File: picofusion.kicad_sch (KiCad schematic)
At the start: 35 parts, among them J1 EAST, J2 WEST, J3 SOUTH, J4 NORTH, U1 W25Q16, U2 RP2040, U3 TLV71333PDQNT, Y1 12MHz

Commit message: schematic: add one more decoupling cap for rp2040
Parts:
- added C?: 1uF, Capacitor_SMD:C_0402_1005Metric, symbol Device:C
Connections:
- net +3V3: now also C?.1
- net GND: now also C?.2
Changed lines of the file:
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@@
   (junction (at 204.47 85.09) (diameter 0) (color 0 0 0 0)
   )
+  (junction (at 137.16 24.13) (diameter 0) (color 0 0 0 0)
+  )
   (junction (at 66.04 24.13) (diameter 0.9144) (color 0 0 0 0)
   )
@@
   (junction (at 179.07 85.09) (diameter 0) (color 0 0 0 0)
   )
+  (junction (at 137.16 36.83) (diameter 0) (color 0 0 0 0)
+  )
   (junction (at 71.12 24.13) (diameter 0.9144) (color 0 0 0 0)
   )
+  (junction (at 60.96 24.13) (diameter 0.9144) (color 0 0 0 0)
+  )
+  (junction (at 106.68 24.13) (diameter 0.9144) (color 0 0 0 0)
+  )
+  (junction (at 91.44 170.18) (diameter 0.9144) (color 0 0 0 0)
+  )
+  (junction (at 19.05 36.83) (diameter 0) (color 0 0 0 0)
+  )
+  (junction (at 106.68 36.83) (diameter 0.9144) (color 0 0 0 0)
+  )
+  (junction (at 199.39 85.09) (diameter 0) (color 0 0 0 0)
+  )
+  (junction (at 41.91 162.56) (diameter 0.9144) (color 0 0 0 0)
+  )
+  (junction (at 114.3 24.13) (diameter 0) (color 0 0 0 0)
+  )
+  (junction (at 19.05 24.13) (diameter 0) (color 0 0 0 0)
+  )
+  (junction (at 78.74 170.18) (diameter 0.9144) (color 0 0 0 0)
+  )
+  (junction (at 81.28 24.13) (diameter 0.9144) (color 0 0 0 0)
+  )
+  (junction (at 129.54 36.83) (diameter 0) (color 0 0 0 0)
+  )
+  (junction (at 18.415 177.8) (diameter 0) (color 0 0 0 0)
+  )
+  (junction (at 46.99 24.13) (diameter 0.9144) (color 0 0 0 0)
+  )
+  (junction (at 44.45 24.13) (diameter 0.9144) (color 0 0 0 0)
+  )
+  (junction (at 121.92 24.13) (diameter 0) (color 0 0 0 0)
+  )
+  (junction (at 83.82 24.13) (diameter 0.9144) (color 0 0 0 0)
+  )
+  (junction (at 179.07 87.63) (diameter 0) (color 0 0 0 0)
+  )
+  (junction (at 68.58 24.13) (diameter 0.9144) (color 0 0 0 0)
+  )
   (junction (at 129.54 24.13) (diameter 0) (color 0 0 0 0)
-  )
-  (junction (at 60.96 24.13) (diameter 0.9144) (color 0 0 0 0)
-  )
-  (junction (at 106.68 24.13) (diameter 0.9144) (color 0 0 0 0)
-  )
-  (junction (at 91.44 170.18) (diameter 0.9144) (color 0 0 0 0)
-  )
-  (junction (at 19.05 36.83) (diameter 0) (color 0 0 0 0)
-  )
-  (junction (at 106.68 36.83) (diameter 0.9144) (color 0 0 0 0)
-  )
-  (junction (at 199.39 85.09) (diameter 0) (color 0 0 0 0)
-  )
-  (junction (at 41.91 162.56) (diameter 0.9144) (color 0 0 0 0)
-  )
-  (junction (at 114.3 24.13) (diameter 0) (color 0 0 0 0)
-  )
-  (junction (at 19.05 24.13) (diameter 0) (color 0 0 0 0)
-  )
-  (junction (at 129.54 36.83) (diameter 0) (color 0 0 0 0)
-  )
-  (junction (at 78.74 170.18) (diameter 0.9144) (color 0 0 0 0)
-  )
-  (junction (at 81.28 24.13) (diameter 0.9144) (color 0 0 0 0)
-  )
-  (junction (at 18.415 177.8) (diameter 0) (color 0 0 0 0)
-  )
-  (junction (at 46.99 24.13) (diameter 0.9144) (color 0 0 0 0)
-  )
-  (junction (at 44.45 24.13) (diameter 0.9144) (color 0 0 0 0)
-  )
-  (junction (at 121.92 24.13) (diameter 0) (color 0 0 0 0)
-  )
-  (junction (at 83.82 24.13) (diameter 0.9144) (color 0 0 0 0)
-  )
-  (junction (at 179.07 87.63) (diameter 0) (color 0 0 0 0)
-  )
-  (junction (at 68.58 24.13) (diameter 0.9144) (color 0 0 0 0)
   )
   (junction (at 114.3 36.83) (diameter 0) (color 0 0 0 0)
@@
     (stroke (width 0) (type solid) (color 0 0 0 0))
   )
+  (wire (pts (xy 137.16 36.83) (xy 129.54 36.83))
+    (stroke (width 0) (type default) (color 0 0 0 0))
+  )
   (wire (pts (xy 19.05 36.83) (xy 25.4 36.83))
     (stroke (width 0) (type solid) (color 0 0 0 0))
@@
     (stroke (width 0) (type default) (color 0 0 0 0))
   )
-  (wire (pts (xy 132.08 21.59) (xy 132.08 24.13))
+  (wire (pts (xy 139.7 21.59) (xy 139.7 24.13))
     (stroke (width 0) (type solid) (color 0 0 0 0))
   )
@@
     (stroke (width 0) (type default) (color 0 0 0 0))
   )
-  (wire (pts (xy 132.08 36.83) (xy 132.08 39.37))
+  (wire (pts (xy 139.7 36.83) (xy 139.7 39.37))
     (stroke (width 0) (type default) (color 0 0 0 0))
   )
@@
     (stroke (width 0) (type solid) (color 0 0 0 0))
   )
+  (wire (pts (xy 129.54 24.13) (xy 137.16 24.13))
+    (stroke (width 0) (type default) (color 0 0 0 0))
+  )
   (wire (pts (xy 25.4 36.83) (xy 31.75 36.83))
     (stroke (width 0) (type solid) (color 0 0 0 0))
@@
     (stroke (width 0) (type default) (color 0 0 0 0))
   )
+  (wire (pts (xy 137.16 24.13) (xy 137.16 26.67))
+    (stroke (width 0) (type default) (color 0 0 0 0))
+  )
   (wire (pts (xy 66.04 24.13) (xy 63.5 24.13))
     (stroke (width 0) (type solid) (color 0 0 0 0))
@@
     (stroke (width 0) (type solid) (color 0 0 0 0))
   )
-  (wire (pts (xy 129.54 24.13) (xy 132.08 24.13))
+  (wire (pts (xy 137.16 24.13) (xy 139.7 24.13))
     (stroke (width 0) (type solid) (color 0 0 0 0))
   )
@@
     (stroke (width 0) (type solid) (color 0 0 0 0))
   )
+  (wire (pts (xy 137.16 34.29) (xy 137.16 36.83))
+    (stroke (width 0) (type default) (color 0 0 0 0))
+  )
   (wire (pts (xy 199.39 82.55) (xy 199.39 85.09))
     (stroke (width 0) (type default) (color 0 0 0 0))
@@
     (stroke (width 0) (type solid) (color 0 0 0 0))
   )
-  (wire (pts (xy 129.54 36.83) (xy 132.08 36.83))
+  (wire (pts (xy 137.16 36.83) (xy 139.7 36.83))
     (stroke (width 0) (type solid) (color 0 0 0 0))
   )
@@
     (effects (font (size 1.27 1.27)) (justify right bottom))
   )
-  (symbol (lib_id "power:+3V3") (at 132.08 21.59 0) (unit 1)
-    (in_bom yes) (on_board yes) (fields_autoplaced)
-    (property "Reference" "#PWR016" (id 0) (at 132.08 25.4 0)
-      (effects (font (size 1.27 1.27)) hide)
-    )
-    (property "Value" "+3V3" (id 1) (at 132.08 16.51 0))
-    (property "Footprint" "" (id 2) (at 132.08 21.59 0)
-      (effects (font (size 1.27 1.27)) hide)
-    )
-    (property "Datasheet" "" (id 3) (at 132.08 21.59 0)
+  (symbol (lib_id "power:+3V3") (at 139.7 21.59 0) (unit 1)
+    (in_bom yes) (on_board yes) (fields_autoplaced)
+    (property "Reference" "#PWR016" (id 0) (at 139.7 25.4 0)
+      (effects (font (size 1.27 1.27)) hide)
+    )
+    (property "Value" "+3V3" (id 1) (at 139.7 16.51 0))
+    (property "Footprint" "" (id 2) (at 139.7 21.59 0)
+      (effects (font (size 1.27 1.27)) hide)
+    )
+    (property "Datasheet" "" (id 3) (at 139.7 21.59 0)
       (effects (font (size 1.27 1.27)) hide)
     )
@@
     (pin "2")
   )
+  (symbol (lib_id "Device:C") (at 137.16 30.48 0) (unit 1)
+    (in_bom yes) (on_board yes)
+    (property "Reference" "C?" (id 0) (at 137.16 27.9399 0)
+      (effects (font (size 1.27 1.27)) (justify left))
+    )
+    (property "Value" "1uF" (id 1) (at 137.16 33.0199 0)
+      (effects (font (size 1.27 1.27)) (justify left))
+    )
+    (property "Footprint" "Capacitor_SMD:C_0402_1005Metric" (id 2) (at 138.1252 34.29 0)
+      (effects (font (size 1.27 1.27)) hide)
+    )
+    (property "Datasheet" "~" (id 3) (at 137.16 30.48 0)
+      (effects (font (size 1.27 1.27)) hide)
+    )
+    (property "LCSC" "C52923" (id 4) (at 137.16 30.48 0)
+      (effects (font (size 1.27 1.27)) hide)
+    )
+    (pin "1")
+    (pin "2")
+  )
   (symbol (lib_id "power:+3V3") (at 172.72 26.67 0) (unit 1)
     (in_bom yes) (on_board yes) (fields_autoplaced)
@@
     (pin "2")
   )
-  (symbol (lib_id "power:GND") (at 132.08 39.37 0) (unit 1)
+  (symbol (lib_id "power:GND") (at 139.7 39.37 0) (unit 1)
     (in_bom yes) (on_board yes)
-    (property "Reference" "#PWR017" (id 0) (at 132.08 45.72 0)
-      (effects (font (size 1.27 1.27)) hide)
-    )
-    (property "Value" "GND" (id 1) (at 135.89 40.64 0))
-    (property "Footprint" "" (id 2) (at 132.08 39.37 0)
-      (effects (font (size 1.27 1.27)) hide)
-    )
-    (property "Datasheet" "" (id 3) (at 132.08 39.37 0)
+    (property "Reference" "#PWR017" (id 0) (at 139.7 45.72 0)
+      (effects (font (size 1.27 1.27)) hide)
+    )
+    (property "Value" "GND" (id 1) (at 143.51 40.64 0))
+    (property "Footprint" "" (id 2) (at 139.7 39.37 0)
+      (effects (font (size 1.27 1.27)) hide)
+    )
+    (property "Datasheet" "" (id 3) (at 139.7 39.37 0)
       (effects (font (size 1.27 1.27)) hide)
     )
@@
       (reference "C24") (unit 1) (value "1uF") (footprint "Capacitor_SMD:C_0402_1005Metric")
     )
+    (path "/7313ba04-79a3-4905-b4a7-933266cdb847"
+      (reference "C?") (unit 1) (value "1uF") (footprint "Capacitor_SMD:C_0402_1005Metric")
+    )
     (path "/83435655-435e-44cf-8361-2ea2525423d1"

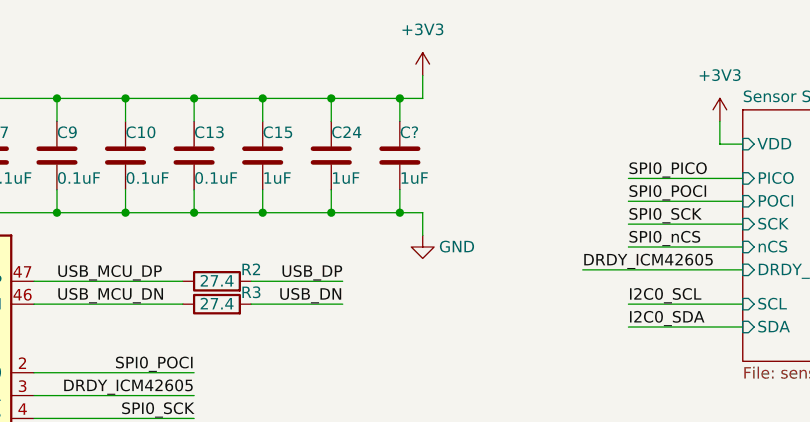
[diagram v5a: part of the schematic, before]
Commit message: schematic/pcb: more routing, add another decoupling cap
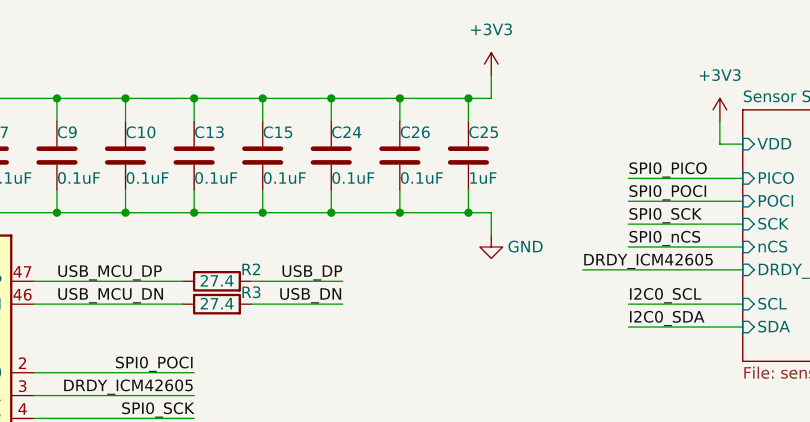
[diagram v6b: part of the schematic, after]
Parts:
- added C26: 0.1uF, Capacitor_SMD:C_0402_1005Metric, symbol Device:C
- C15, C24: value 1uF -> 0.1uF
- gave numbers to parts that had none: 1
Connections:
- net +3V3: now also C26.1
- net GND: now also C26.2
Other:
- moved on the sheet: C25

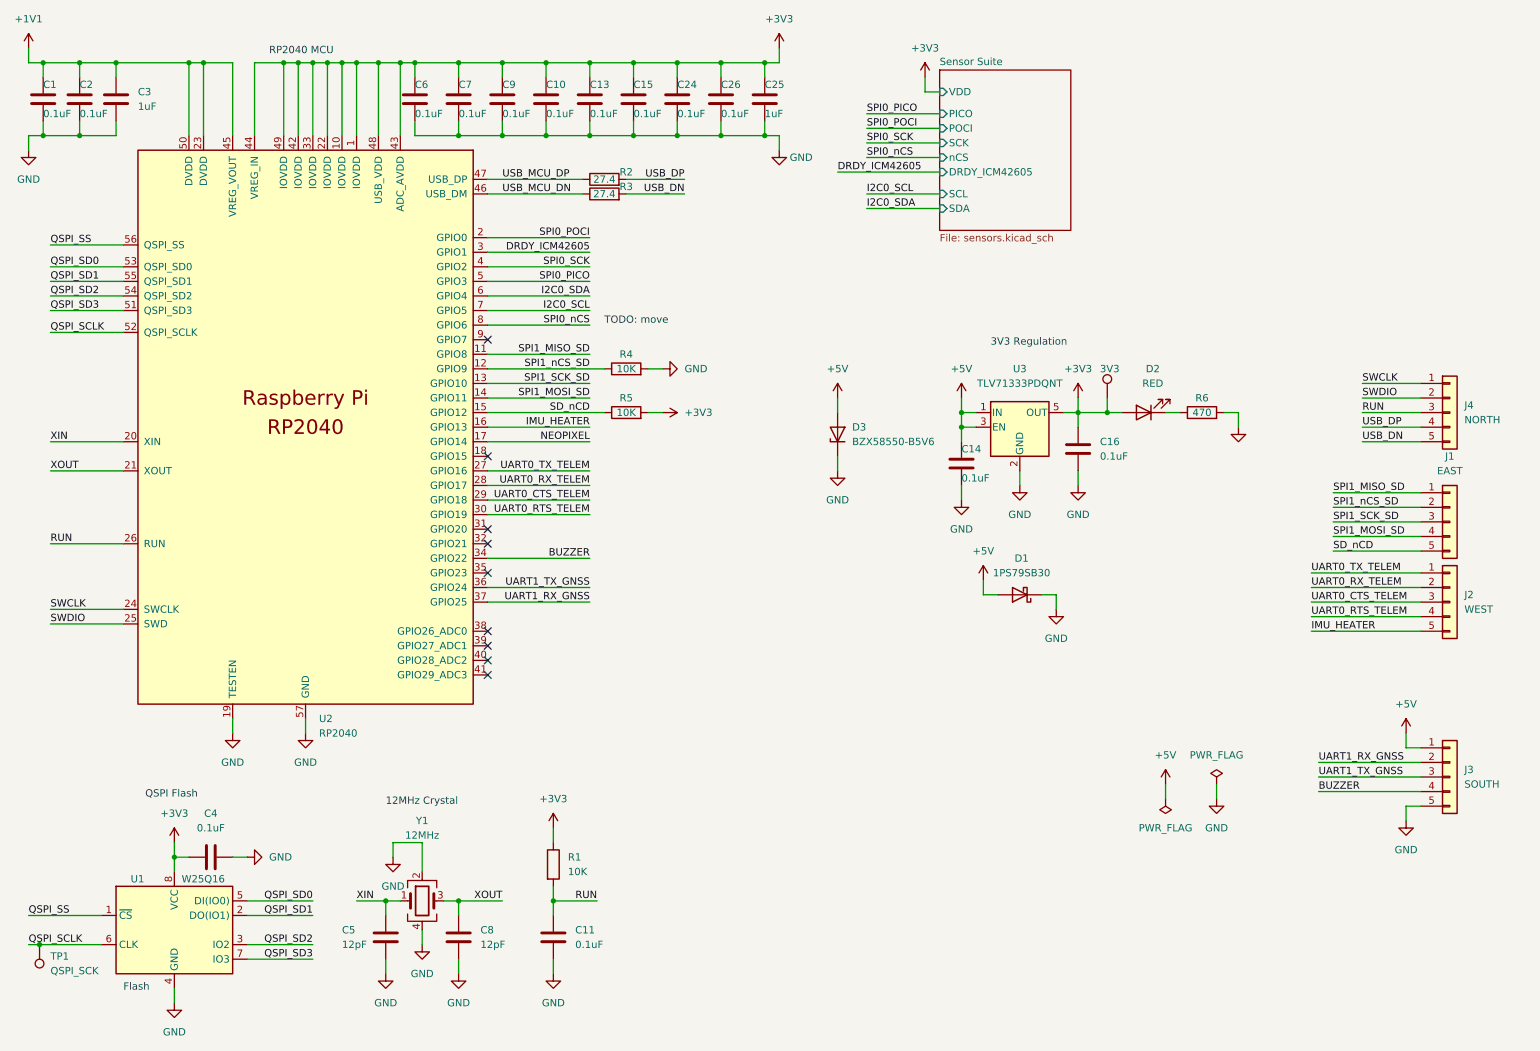
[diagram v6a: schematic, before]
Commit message: Add new CAN transceiver and castellated holes
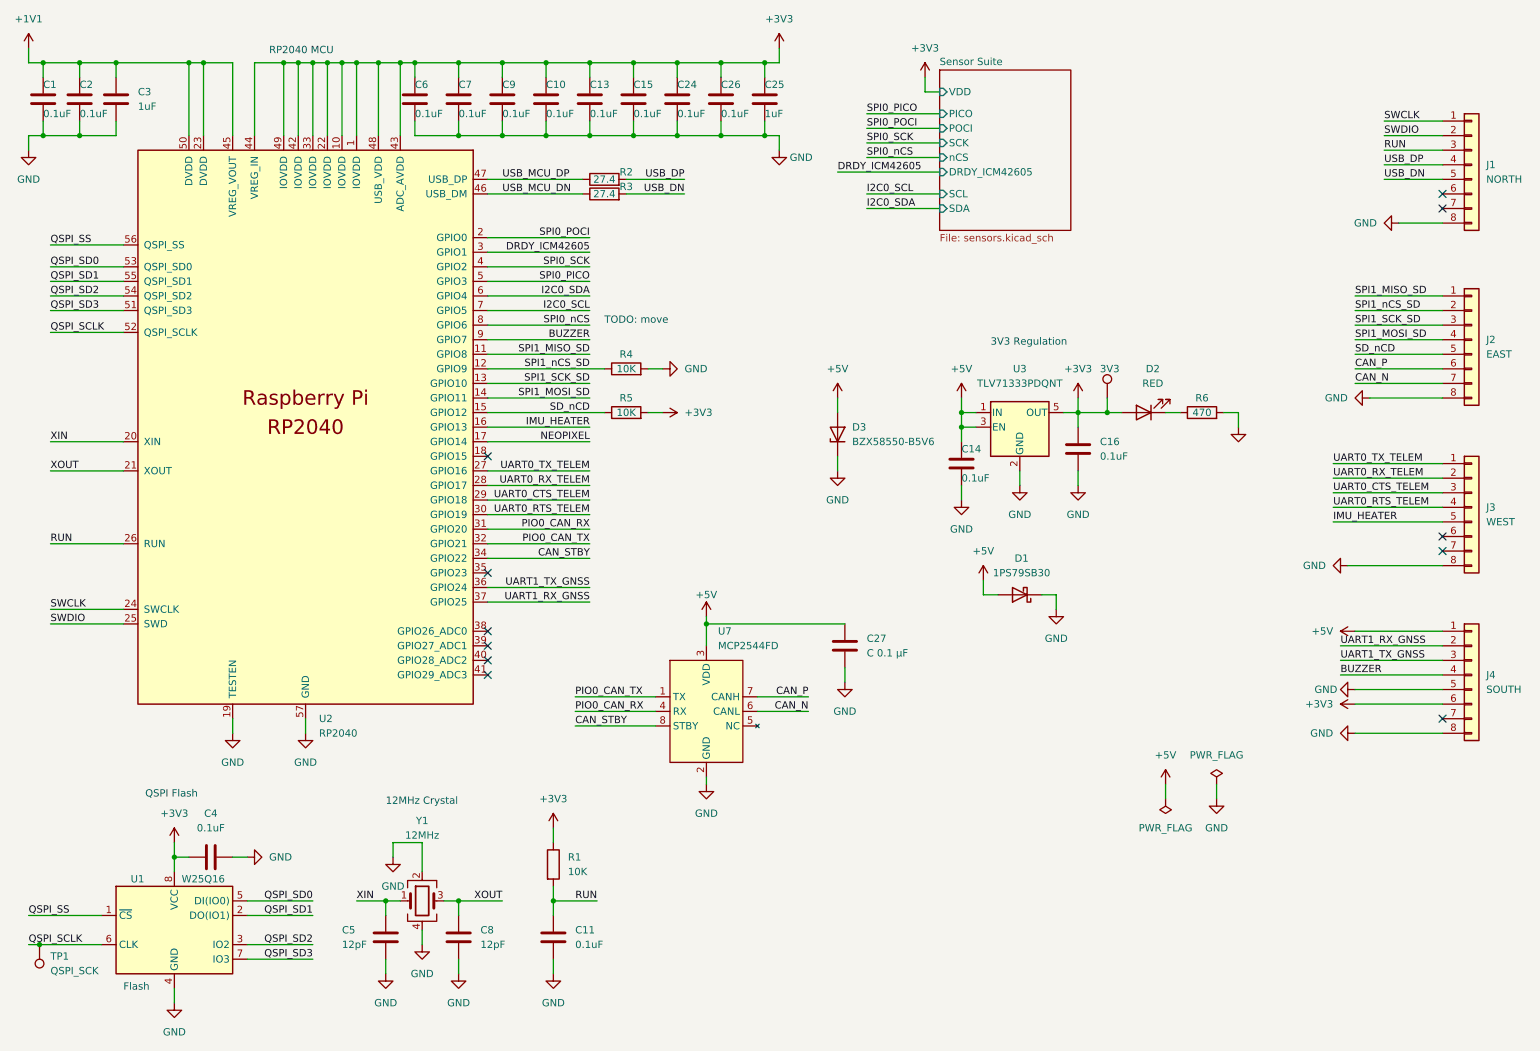
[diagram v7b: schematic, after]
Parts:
- removed J1: EAST, Connector_PinHeader_2.54mm:PinHeader_1x05_P2.54mm_Vertical, symbol Connector_Generic:Conn_01x05
- removed J2: WEST, Connector_PinHeader_2.54mm:PinHeader_1x05_P2.54mm_Vertical, symbol Connector_Generic:Conn_01x05
- removed J3: SOUTH, Connector_PinHeader_2.54mm:PinHeader_1x05_P2.54mm_Vertical, symbol Connector_Generic:Conn_01x05
- removed J4: NORTH, Connector_PinHeader_2.54mm:PinHeader_1x05_P2.54mm_Vertical, symbol Connector_Generic:Conn_01x05
- added C27: C 0.1 µF, Capacitor_SMD:C_0402_1005Metric, symbol Device:C
- added J1: NORTH, picofusion_stamp:Castellated_1x8_P2.54mm_Vertical, symbol Connector_Generic:Conn_01x08
- added J2: EAST, picofusion_stamp:Castellated_1x8_P2.54mm_Vertical, symbol Connector_Generic:Conn_01x08
- added J3: WEST, picofusion_stamp:Castellated_1x8_P2.54mm_Vertical, symbol Connector_Generic:Conn_01x08
- added J4: SOUTH, picofusion_stamp:Castellated_1x8_P2.54mm_Vertical, symbol Connector_Generic:Conn_01x08
- added U7: MCP2544FD, Package_SO:SOP-8_3.9x4.9mm_P1.27mm, symbol mcp2544fd:MCP2544FD
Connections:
- net +3V3: now also J4.6 (Pin_6)
- net +5V: now also C27.1, J4.1 (Pin_1), U7.3 (VDD)
- net BUZZER: now also U2.9 (GPIO7), J4.4 (Pin_4); no longer U2.34 (GPIO22)
- net GND: now also C27.2, J1.8 (Pin_8), J2.8 (Pin_8), J3.8 (Pin_8), J4.5 (Pin_5), J4.8 (Pin_8), U7.2 (GND)
- net IMU_HEATER: now also J3.5 (Pin_5)
- net RUN: now also J1.3 (Pin_3)
- net SD_nCD: now also J2.5 (Pin_5)
- net SPI1_MISO_SD: now also J2.1 (Pin_1)
- net SPI1_MOSI_SD: now also J2.4 (Pin_4)
- net SPI1_SCK_SD: now also J2.3 (Pin_3)
- net SPI1_nCS_SD: now also J2.2 (Pin_2)
- net SWCLK: now also J1.1 (Pin_1)
- net SWDIO: now also J1.2 (Pin_2)
- net UART0_CTS_TELEM: now also J3.3 (Pin_3)
- net UART0_RTS_TELEM: now also J3.4 (Pin_4)
- net UART0_RX_TELEM: now also J3.2 (Pin_2)
- net UART0_TX_TELEM: now also J3.1 (Pin_1)
- net UART1_RX_GNSS: now also J4.2 (Pin_2)
- net UART1_TX_GNSS: now also J4.3 (Pin_3)
- net USB_DN: now also J1.5 (Pin_5)
- net USB_DP: now also J1.4 (Pin_4)
- net PIO0_CAN_RX: now reaches U2.31 (GPIO20)
- net PIO0_CAN_RX: now also U7.4 (RX)
- net PIO0_CAN_TX: now reaches U2.32 (GPIO21)
- net PIO0_CAN_TX: now also U7.1 (TX)
- new net CAN_N: J2.7 (Pin_7), U7.6 (CANL)
- new net CAN_P: J2.6 (Pin_6), U7.7 (CANH)
- new net CAN_STBY: U2.34 (GPIO22), U7.8 (STBY)
- no-connect marks 9 -> 11
